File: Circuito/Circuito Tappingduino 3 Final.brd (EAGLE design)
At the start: 90.5 x 59.5 mm, 67 parts, among them IC1 LM324N

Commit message: 100% 17 vias - Tamaños correctos
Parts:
- moved R20 28.5 mm to (51.5, 60.8), turned to 0 degrees
- moved R17 18.0 mm to (19.5, 58.2), turned to 270 degrees
- moved R9 14.0 mm to (31.5, 58.2), turned to 90 degrees
- moved R12 13.8 mm to (51.5, 56.5), turned to 180 degrees
- moved R18 13.5 mm to (20.8, 12.2), turned to 0 degrees
- moved R13 13.5 mm to (68.2, 47.2)
- moved R4 13.3 mm to (25.8, 58.2)
- moved R3 12.8 mm to (18.0, 42.5)
- moved R19 11.2 mm to (55.8, 41.5)
- moved R11 10.9 mm to (55.8, 45.5)
- moved SCH2 9.55 mm to (70.5, 59.5)
- moved SCH3 9.41 mm to (84.0, 59.2)
- moved R14 8.75 mm to (44.8, 45.8)
- moved PHONES 8.00 mm to (13.0, 22.8)
- moved R2 6.60 mm to (78.5, 45.0)
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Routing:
- net VCC: track 154.8 -> 204.7 mm, vias 0 -> 2
- net N$17: track 39.6 -> 88.7 mm, vias 1 -> 0
- net N$18: track 41.1 -> 80.2 mm, vias 0 -> 3
- net N$37: track 100.2 -> 66.8 mm, vias 5 -> 0
- net N$7: track 55.1 -> 84.7 mm
- net N$8: track 198.9 -> 175.4 mm
- net N$13: track 66.5 -> 89.5 mm, vias 2 -> 1
- net N$9: track 22.7 -> 42.7 mm, vias 0 -> 1
- net N$11: track 37.4 -> 57.4 mm
- net N$19: track 34.4 -> 54.2 mm
- net N$3: track 17.6 -> 4.73 mm
- net N$24: track 25.2 -> 34.4 mm, vias 1 -> 0
- net N$28: track 42.6 -> 50.5 mm, vias 1 -> 0
- net N$14: track 18.5 -> 26.1 mm, vias 0 -> 1
- net N$20: track 24.5 -> 17.2 mm, vias 2 -> 0
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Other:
- board size 90.5 x 59.5 mm -> 90.5 x 69 mm

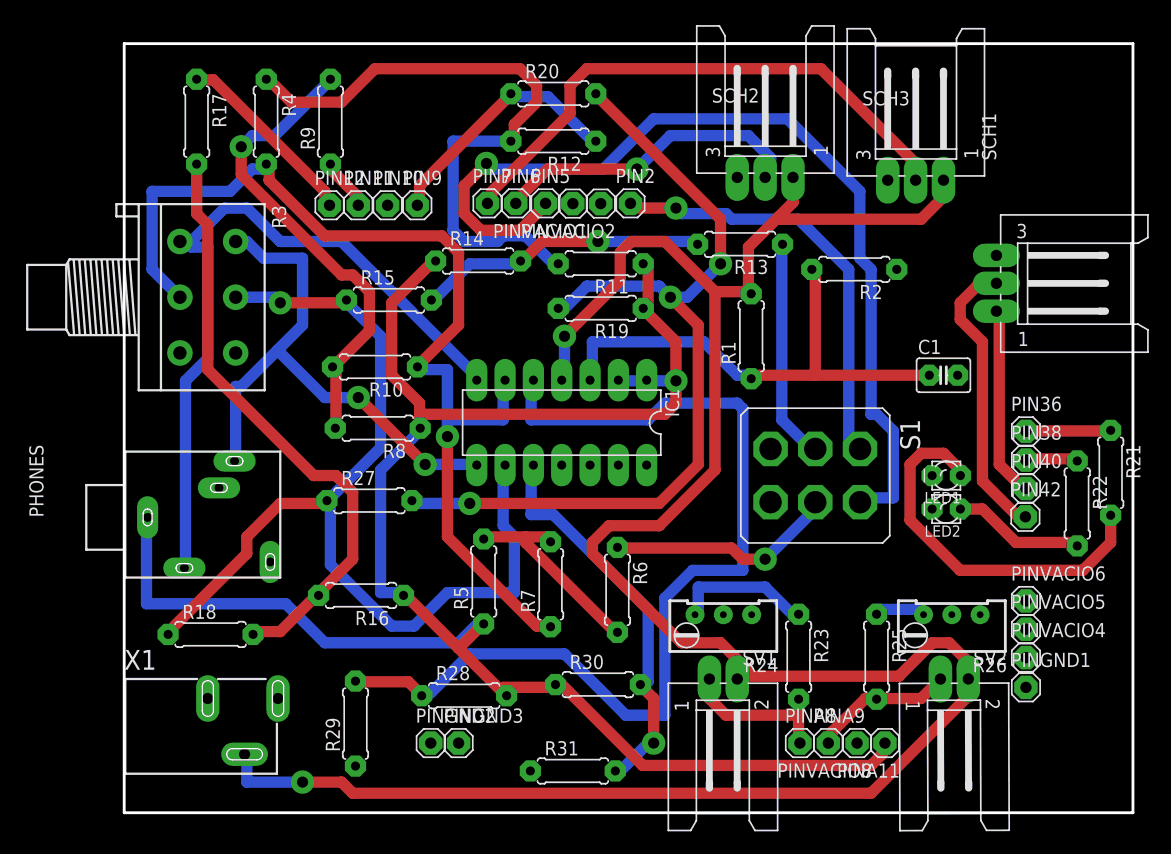
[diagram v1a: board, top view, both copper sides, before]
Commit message: Versiones definitivas del circuito
brd, sch, pdfs de bottom, top(mirror) y hoja completa en tamaño carta.
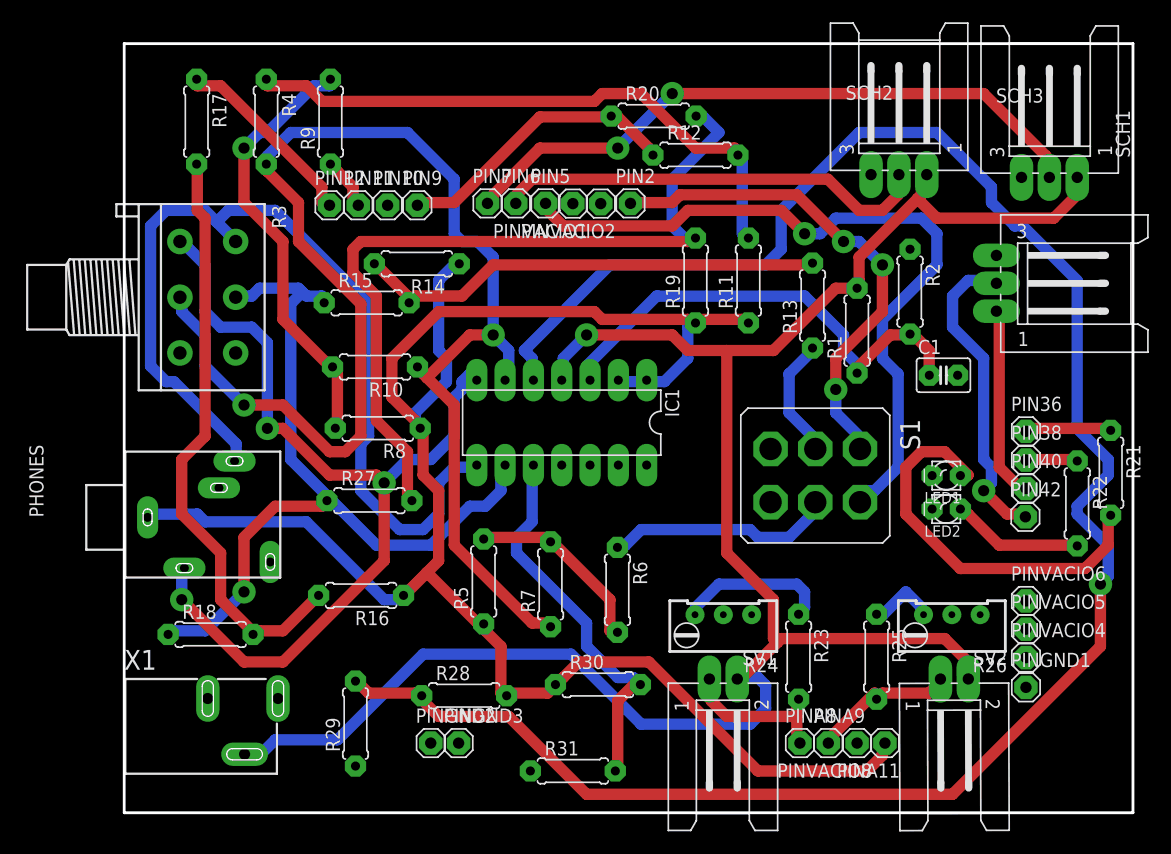
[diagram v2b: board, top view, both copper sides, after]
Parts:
- moved R11 13.3 mm to (69.0, 44.0), turned to 90 degrees
- moved R12 12.8 mm to (64.2, 55.2), turned to 0 degrees
- moved SCH2 12.0 mm to (82.5, 59.8)
- moved SCH3 12.0 mm to (96.0, 59.5)
- moved R1 9.51 mm to (78.8, 39.5)
- moved R20 9.22 mm to (60.5, 58.8)
- moved R19 8.86 mm to (64.2, 44.0), turned to 90 degrees
- moved R13 8.51 mm to (74.8, 41.8), turned to 90 degrees
- moved R14 5.51 mm to (39.2, 45.5), turned to 180 degrees
- moved R2 5.39 mm to (83.5, 43.0), turned to 270 degrees
- moved R15 2.02 mm to (34.8, 42.0)
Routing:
- net N$17: track 88.7 -> 182.2 mm, vias 0 -> 1
- net N$4: track 93.9 -> 130.4 mm, vias 1 -> 2
- net N$30: track 49.8 -> 84.5 mm, vias 2 -> 0
- net VCC: track 204.7 -> 173.6 mm, vias 2 -> 1
- net N$7: track 84.7 -> 67.7 mm
- net N$37: track 66.8 -> 83.5 mm, vias 0 -> 3
- net N$14: track 26.1 -> 42.5 mm, vias 1 -> 0
- net N$13: track 89.5 -> 73.4 mm
- net N$29: track 28.7 -> 39.2 mm, vias 1 -> 0
- net N$18: track 80.2 -> 71.4 mm, vias 3 -> 0
- net N$15: track 19.9 -> 11.3 mm
- net N$28: track 50.5 -> 58.9 mm, vias 0 -> 2
- net N$8: track 175.4 -> 168.5 mm, vias 1 -> 0
- net N$16: track 39.3 -> 45.2 mm, vias 1 -> 3
- net N$9: track 42.7 -> 39.3 mm
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
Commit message: Version final del circuito
Lo vuelvo a subir porque no estaba segura de haber guardado el archivo de eagle que tiene ya las vias adicionales en la resistencia variable que tenia los pads muy chicos.
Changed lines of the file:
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@@
 <grid distance="0.25" unitdist="mm" unit="mm" style="lines" multiple="1" display="yes" altdistance="0.025" altunitdist="inch" altunit="inch"/>
 <layers>
-<layer number="1" name="Top" color="4" fill="1" visible="yes" active="yes"/>
+<layer number="1" name="Top" color="4" fill="1" visible="no" active="yes"/>
 <layer number="2" name="Route2" color="1" fill="3" visible="no" active="no"/>
 <layer number="3" name="Route3" color="4" fill="3" visible="no" active="no"/>
@@
 <layer number="17" name="Pads" color="2" fill="1" visible="yes" active="yes"/>
 <layer number="18" name="Vias" color="2" fill="1" visible="yes" active="yes"/>
-<layer number="19" name="Unrouted" color="6" fill="1" visible="yes" active="yes"/>
-<layer number="20" name="Dimension" color="15" fill="1" visible="yes" active="yes"/>
-<layer number="21" name="tPlace" color="7" fill="1" visible="yes" active="yes"/>
-<layer number="22" name="bPlace" color="7" fill="1" visible="yes" active="yes"/>
-<layer number="23" name="tOrigins" color="15" fill="1" visible="yes" active="yes"/>
-<layer number="24" name="bOrigins" color="15" fill="1" visible="yes" active="yes"/>
-<layer number="25" name="tNames" color="7" fill="1" visible="yes" active="yes"/>
-<layer number="26" name="bNames" color="7" fill="1" visible="yes" active="yes"/>
-<layer number="27" name="tValues" color="7" fill="1" visible="yes" active="yes"/>
-<layer number="28" name="bValues" color="7" fill="1" visible="yes" active="yes"/>
+<layer number="19" name="Unrouted" color="6" fill="1" visible="no" active="yes"/>
+<layer number="20" name="Dimension" color="15" fill="1" visible="no" active="yes"/>
+<layer number="21" name="tPlace" color="7" fill="1" visible="no" active="yes"/>
+<layer number="22" name="bPlace" color="7" fill="1" visible="no" active="yes"/>
+<layer number="23" name="tOrigins" color="15" fill="1" visible="no" active="yes"/>
+<layer number="24" name="bOrigins" color="15" fill="1" visible="no" active="yes"/>
+<layer number="25" name="tNames" color="7" fill="1" visible="no" active="yes"/>
+<layer number="26" name="bNames" color="7" fill="1" visible="no" active="yes"/>
+<layer number="27" name="tValues" color="7" fill="1" visible="no" active="yes"/>
+<layer number="28" name="bValues" color="7" fill="1" visible="no" active="yes"/>
 <layer number="29" name="tStop" color="7" fill="3" visible="no" active="yes"/>
 <layer number="30" name="bStop" color="7" fill="6" visible="no" active="yes"/>
@@
 <layer number="39" name="tKeepout" color="4" fill="11" visible="no" active="yes"/>
 <layer number="40" name="bKeepout" color="1" fill="11" visible="no" active="yes"/>
-<layer number="41" name="tRestrict" color="4" fill="10" visible="yes" active="yes"/>
-<layer number="42" name="bRestrict" color="1" fill="10" visible="yes" active="yes"/>
-<layer number="43" name="vRestrict" color="2" fill="10" visible="yes" active="yes"/>
+<layer number="41" name="tRestrict" color="4" fill="10" visible="no" active="yes"/>
+<layer number="42" name="bRestrict" color="1" fill="10" visible="no" active="yes"/>
+<layer number="43" name="vRestrict" color="2" fill="10" visible="no" active="yes"/>
 <layer number="44" name="Drills" color="7" fill="1" visible="no" active="yes"/>
 <layer number="45" name="Holes" color="7" fill="1" visible="no" active="yes"/>
@@
 <vertex x="103.5" y="65.25"/>
 </polygon>
+<wire x1="93.9" y1="7.5" x2="87.25" y2="14.02" width="0" layer="19" extent="1-1"/>
+<wire x1="66.75" y1="14.02" x2="52.25" y2="27.44" width="0" layer="19" extent="1-1"/>
 </signal>
 <signal name="N$1">
@@
 <wire x1="58.674" y1="8.382" x2="59.31" y2="7.75" width="1.016" layer="16"/>
 </signal>
+<signal name="N$12">
+<via x="64.25" y="14" extent="1-16" drill="1"/>
+</signal>
+<signal name="N$33">
+<via x="66.75" y="14" extent="1-16" drill="1"/>
+</signal>
+<signal name="N$35">
+<via x="69.25" y="14" extent="1-16" drill="1"/>
+</signal>
+<signal name="N$36">
+<via x="84.75" y="14" extent="1-16" drill="1"/>
+</signal>
+<signal name="N$38">
+<via x="87.25" y="14" extent="1-16" drill="1"/>
+</signal>
+<signal name="N$39">
+<via x="89.75" y="14" extent="1-16" drill="1"/>
+</signal>
 </signals>
